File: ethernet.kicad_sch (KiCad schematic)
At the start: 57 parts

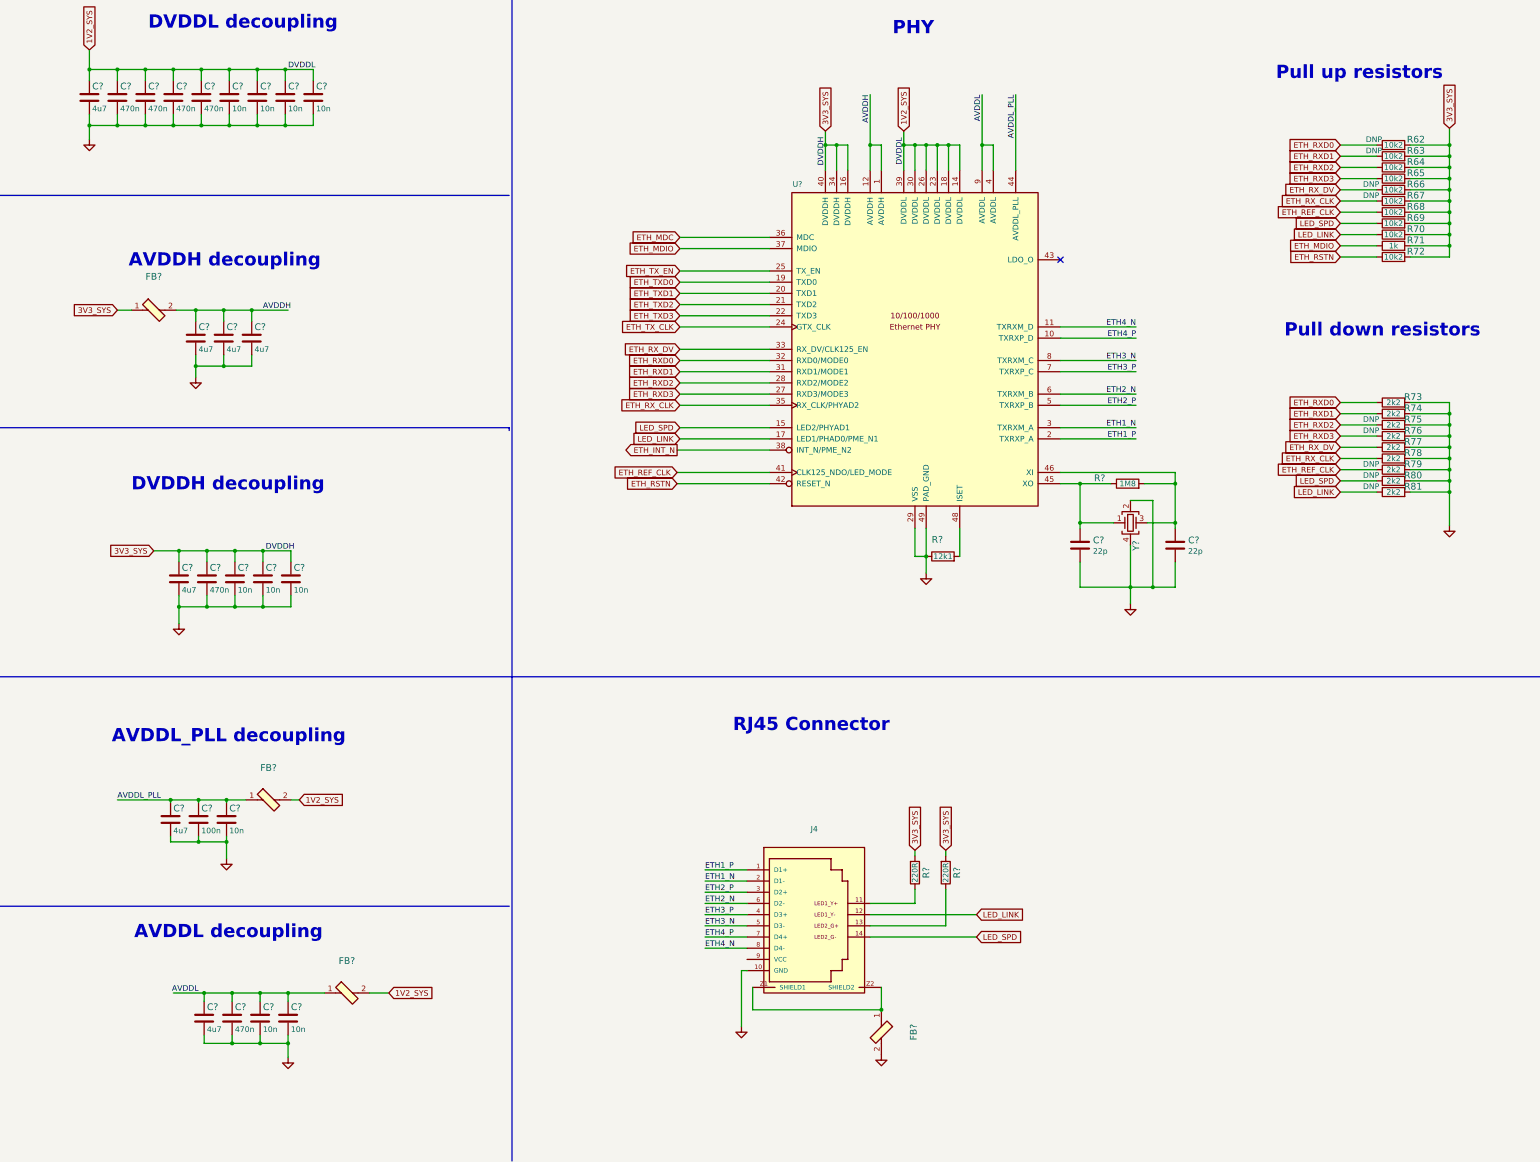
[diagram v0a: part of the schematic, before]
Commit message: Added EN pullup for TPS54561 to avoid disabling by touch
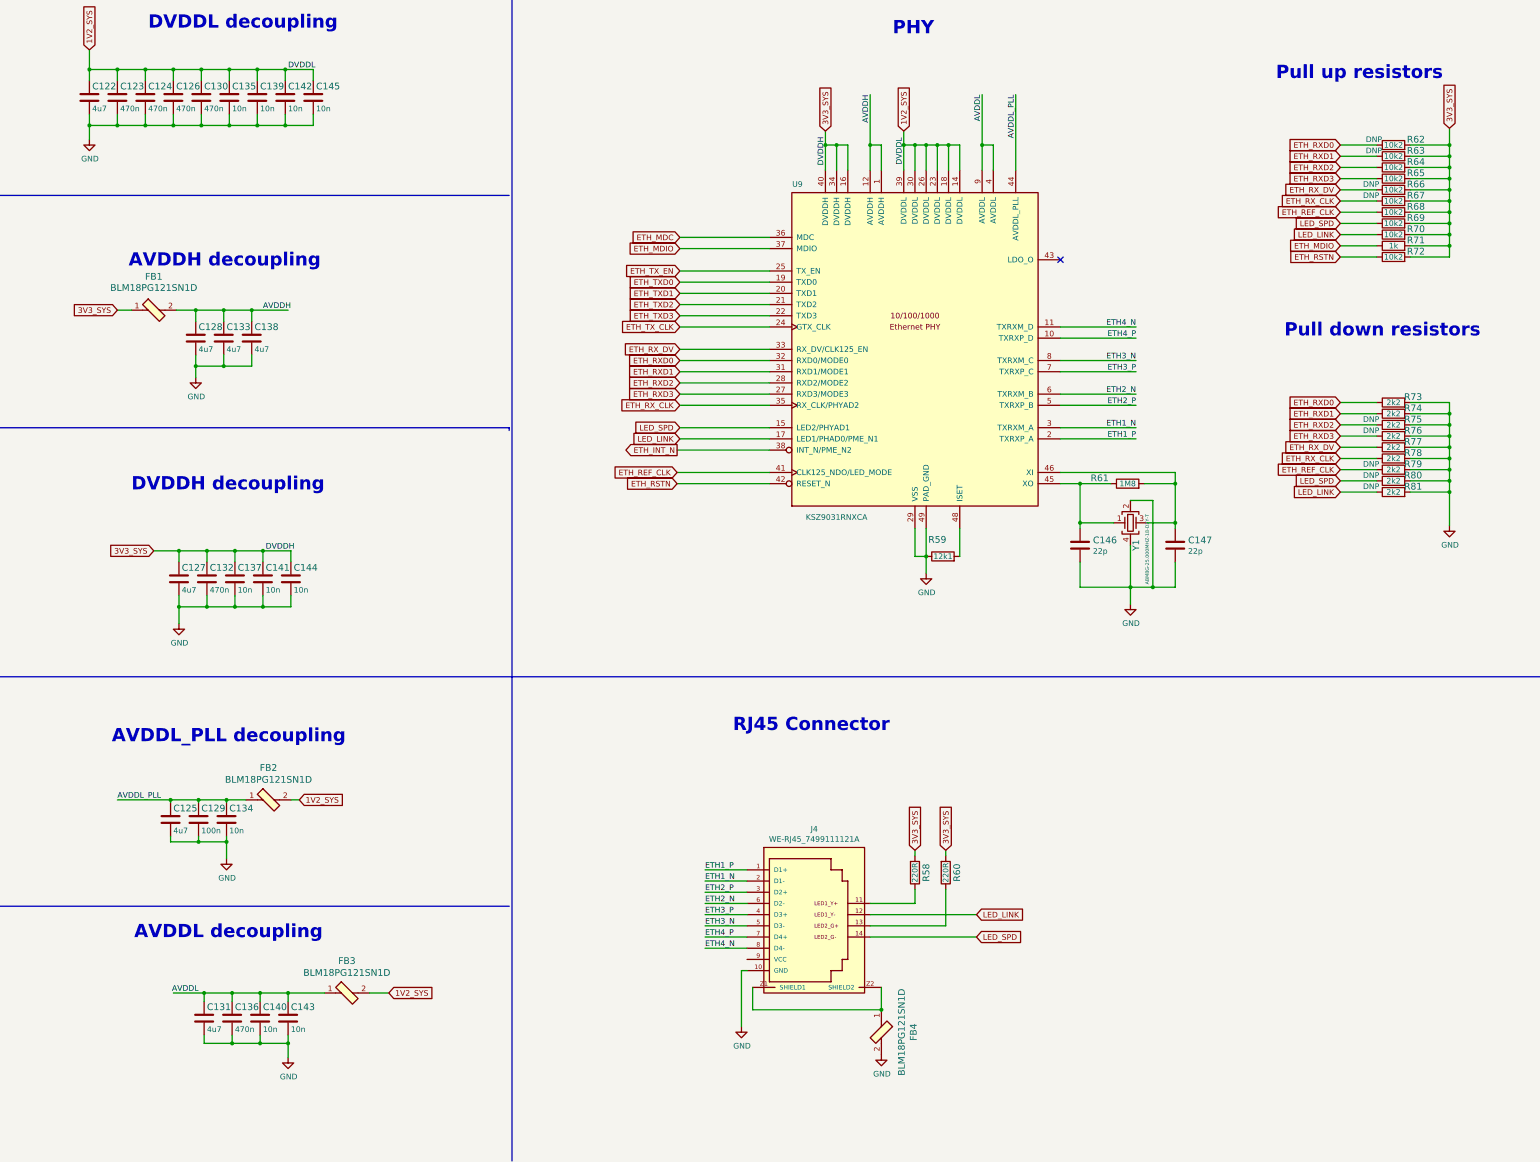
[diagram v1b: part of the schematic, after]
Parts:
- C122, C125, C127, C128, C131: renamed from C?; value (none) -> C_4u7_0402; footprint (none) -> ddr5-testboard-footprints:0402-cap
- C123, C124, C126, C132, C136: renamed from C?; value (none) -> C_470n_0402; footprint (none) -> ddr5-testboard-footprints:0402-cap
- C129: renamed from C?; value (none) -> C_100n_0402; footprint (none) -> ddr5-testboard-footprints:0402-cap
- C130, C133, C134, C135, C137, C138, C139, C140, C141, C142, C143, C144, C145: renamed from C?; value (none) -> C_10n_0402; footprint (none) -> ddr5-testboard-footprints:0402-cap
- C146, C147: renamed from C?; value (none) -> C_22p_0402; footprint (none) -> ddr5-testboard-footprints:0402-cap
- FB1, FB2, FB3, FB4: renamed from FB?; value (none) -> BLM18PG121SN1D; footprint (none) -> ddr5-testboard-footprints:0603-res
- J4: value (none) -> WE-RJ45_7499111121A; footprint (none) -> ddr5-testboard-footprints:7499111121A
- R58, R60: renamed from R?; value (none) -> R_220R_0402; footprint (none) -> ddr5-testboard-footprints:0402-res
- R59: renamed from R?; value (none) -> R_12k1_0402; footprint (none) -> ddr5-testboard-footprints:0402-res
- R61: renamed from R?; value (none) -> R_1M8_0402; footprint (none) -> ddr5-testboard-footprints:0402-res
- R62, R63, R64, R65, R66, R67, R68, R69, R70, R72: value (none) -> R_10k2_0402; footprint (none) -> ddr5-testboard-footprints:0402-res
- R71: value (none) -> R_1k_0402; footprint (none) -> ddr5-testboard-footprints:0402-res
- R73, R74, R75, R76, R77, R78, R79, R80, R81: value (none) -> R_2k2_0402; footprint (none) -> ddr5-testboard-footprints:0402-res
- U9: renamed from U?; value (none) -> KSZ9031RNXCA; footprint (none) -> ddr5-testboard-footprints:QFN-48-Microchip-QFN77-48LD-PL-2
- Y1: renamed from Y?; value (none) -> ABM8G-25.000MHZ-18-D2Y-T; footprint (none) -> ddr5-testboard-footprints:KX-7

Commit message: Update naming convention
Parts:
- C122, C125, C127, C128, C131, C133, C138: footprint ddr5-testboard-footprints:0402-cap -> data-center-rdimm-ddr5-tester-footprints:0402-cap; symbol ddr5-testboard:C_4u7_0402 -> data-center-rdimm-ddr5-tester:C_4u7_0402
- C123, C124, C126, C130, C132, C136: footprint ddr5-testboard-footprints:0402-cap -> data-center-rdimm-ddr5-tester-footprints:0402-cap; symbol ddr5-testboard:C_470n_0402 -> data-center-rdimm-ddr5-tester:C_470n_0402
- C129: footprint ddr5-testboard-footprints:0402-cap -> data-center-rdimm-ddr5-tester-footprints:0402-cap; symbol ddr5-testboard:C_100n_0402_16V -> data-center-rdimm-ddr5-tester:C_100n_0402_16V
- C134, C135, C137, C139, C140, C141, C142, C143, C144, C145: footprint ddr5-testboard-footprints:0402-cap -> data-center-rdimm-ddr5-tester-footprints:0402-cap; symbol ddr5-testboard:C_10n_0402 -> data-center-rdimm-ddr5-tester:C_10n_0402
- C146, C147: footprint ddr5-testboard-footprints:0402-cap -> data-center-rdimm-ddr5-tester-footprints:0402-cap; symbol ddr5-testboard:C_22p_0402 -> data-center-rdimm-ddr5-tester:C_22p_0402
- FB1, FB2, FB3, FB4: footprint ddr5-testboard-footprints:0603-res -> data-center-rdimm-ddr5-tester-footprints:0603-res; symbol ddr5-testboard:BLM18PG121SN1D -> data-center-rdimm-ddr5-tester:BLM18PG121SN1D
- J4: footprint ddr5-testboard-footprints:7499111121A -> data-center-rdimm-ddr5-tester-footprints:7499111121A; symbol ddr5-testboard:WE-RJ45_7499111121A -> data-center-rdimm-ddr5-tester:WE-RJ45_7499111121A
- R58, R60: footprint ddr5-testboard-footprints:0402-res -> data-center-rdimm-ddr5-tester-footprints:0402-res; symbol ddr5-testboard:R_220R_0402 -> data-center-rdimm-ddr5-tester:R_220R_0402
- R59: footprint ddr5-testboard-footprints:0402-res -> data-center-rdimm-ddr5-tester-footprints:0402-res; symbol ddr5-testboard:R_12k1_0402 -> data-center-rdimm-ddr5-tester:R_12k1_0402
- R61: footprint ddr5-testboard-footprints:0402-res -> data-center-rdimm-ddr5-tester-footprints:0402-res; symbol ddr5-testboard:R_1M8_0402 -> data-center-rdimm-ddr5-tester:R_1M8_0402
- R62, R63, R64, R65, R66, R67, R68, R69, R70, R72: footprint ddr5-testboard-footprints:0402-res -> data-center-rdimm-ddr5-tester-footprints:0402-res; symbol ddr5-testboard:R_10k2_0402 -> data-center-rdimm-ddr5-tester:R_10k2_0402
- R71: footprint ddr5-testboard-footprints:0402-res -> data-center-rdimm-ddr5-tester-footprints:0402-res; symbol ddr5-testboard:R_1k_0402 -> data-center-rdimm-ddr5-tester:R_1k_0402
- R73, R74, R75, R76, R77, R78, R79, R80, R81: footprint ddr5-testboard-footprints:0402-res -> data-center-rdimm-ddr5-tester-footprints:0402-res; symbol ddr5-testboard:R_2k2_0402 -> data-center-rdimm-ddr5-tester:R_2k2_0402
- U9: footprint ddr5-testboard-footprints:QFN-48-Microchip-QFN77-48LD-PL-2 -> data-center-rdimm-ddr5-tester-footprints:QFN-48-Microchip-QFN77-48LD-PL-2; symbol ddr5-testboard:KSZ9031RNXCA -> data-center-rdimm-ddr5-tester:KSZ9031RNXCA
- Y1: footprint ddr5-testboard-footprints:KX-7 -> data-center-rdimm-ddr5-tester-footprints:KX-7; symbol ddr5-testboard:ABM8G-25.000MHZ-18-D2Y-T -> data-center-rdimm-ddr5-tester:ABM8G-25.000MHZ-18-D2Y-T
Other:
- title: DDR5 Tester -> Data Center RDIMM DDR5 Tester
